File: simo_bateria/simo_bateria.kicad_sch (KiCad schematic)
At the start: 5 parts, among them J1 CONECTOR BATERIA( 8V), J2 CONECTOR PLUG IN (5V), U3 conversor_dc

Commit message: update placa simo bateria
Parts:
- BAT2: DIGIKEY (none) -> BK-18650-PC2-ND
- U3: NUMBER IC (none) -> 2156-LM2596SX-ADJ-TI-ND
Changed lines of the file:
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@@
       (effects (font (size 1.27 1.27)) hide)
     )
-    (property "Datasheet" "" (id 3) (at 84.582 53.34 0)
+    (property "Datasheet" "https://rocelec.widen.net/view/pdf/gzjkwe71dm/lm2596.pdf?t.download=true&u=5oefqw" (id 3) (at 84.582 53.34 0)
+      (effects (font (size 1.27 1.27)) hide)
+    )
+    (property "NUMBER IC" "2156-LM2596SX-ADJ-TI-ND" (id 4) (at 84.582 53.34 0)
       (effects (font (size 1.27 1.27)) hide)
     )
@@
       (effects (font (size 1.27 1.27)) hide)
     )
-    (property "Datasheet" "" (id 3) (at 45.466 62.357 0)
+    (property "Datasheet" "https://www.memoryprotectiondevices.com/datasheets/BK-18650-PC2-datasheet.pdf" (id 3) (at 45.466 62.357 0)
       (effects (font (size 1.27 1.27)) hide)
     )
+    (property "DIGIKEY" "BK-18650-PC2-ND" (id 4) (at 45.466 62.357 0)
+      (effects (font (size 1.27 1.27)) hide)
+    )

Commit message: Se hizo refactory del proyecto simo_bateria
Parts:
- removed BAT1, BAT2: bateria, Battery:BatteryHolder_MPD_BH-18650-PC2, symbol simo_bateria:bateria
- removed U3: conversor_dc, simo_bateria:conversor_dc_dc, symbol simo_bateria:conversor_dc
- added 11: conversor_dc_1_1, symbol simo_bateria:conversor_dc_1_1
- added BT1, BT2: Battery_Cell, simo_bateria:BatteryHolder_MPD_BH-18650-PC2, symbol Device:Battery_Cell
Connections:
- net at J1.2 (Pin_2): now also 11.1 (VIN-), BT2.2 (-)
- net at J2.1 (Pin_1): now also 11.2 (VOUT-)
- net at J2.2 (Pin_2): now also 11.4 (VOUT+)
- net at J1.1 (Pin_1): now also 11.3 (VIN+), BT1.1 (+)
- new net: BT1.2 (-), BT2.1 (+)
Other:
- note added: "Baterias en serie. 8,4 V MAX"
- note added: "PLUGIN ALIMENTA PLACA ELEMON"
- moved on the sheet: J1

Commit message: update simo_bateria
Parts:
- 11: footprint (none) -> simo_bateria:conversor_dc_dc
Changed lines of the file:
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@@
     (property "Reference" "11" (id 0) (at 95.377 50.8 0))
     (property "Value" "conversor_dc_1_1" (id 1) (at 95.377 53.34 0))
-    (property "Footprint" "" (id 2) (at 84.582 53.34 0)
+    (property "Footprint" "simo_bateria:conversor_dc_dc" (id 2) (at 84.582 53.34 0)
       (effects (font (size 1.27 1.27)) hide)
     )
@@
     )
     (path "/11fd5699-de88-4095-a2ac-268b5557a2ec"
-      (reference "11") (unit 1) (value "conversor_dc_1_1") (footprint "")
+      (reference "11") (unit 1) (value "conversor_dc_1_1") (footprint "simo_bateria:conversor_dc_dc")
     )
     (path "/0e1c8888-24a9-448a-8220-c54ef612d9ed"

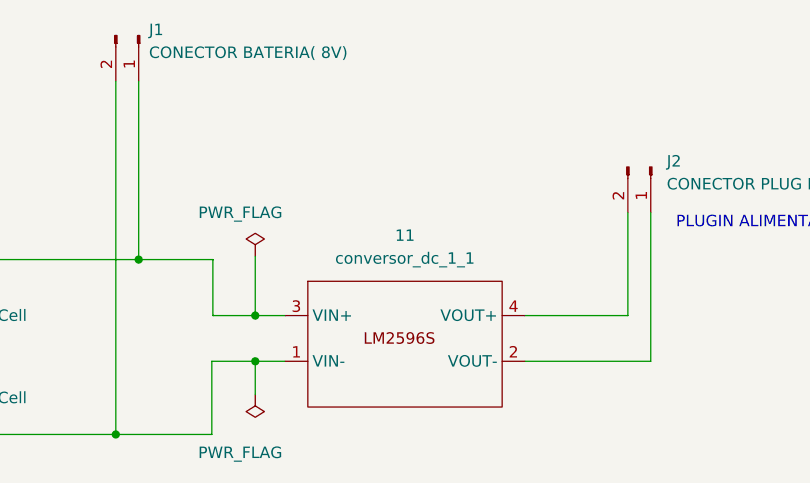
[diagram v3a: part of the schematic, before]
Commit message: update en ambas placas. Cambio de formato de carpetas. Footprint asignado pero modelos 3d aun no.
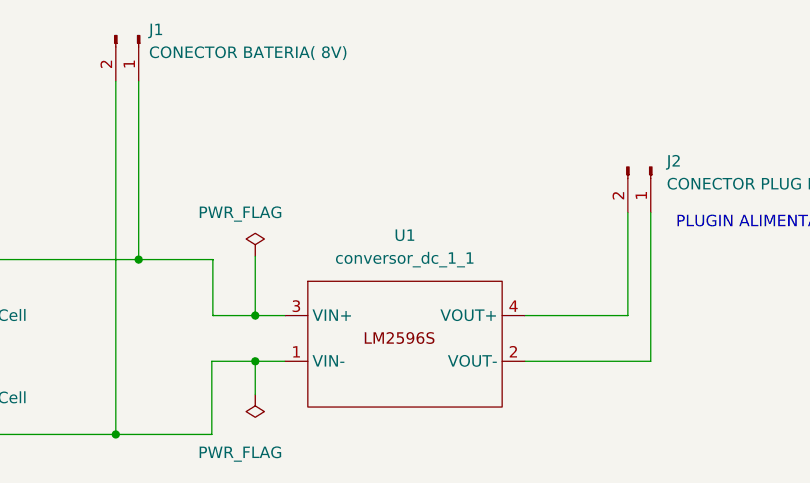
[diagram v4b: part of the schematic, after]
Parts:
- J1, J2: footprint Connector_JST:JST_EH_B2B-EH-A_1x02_P2.50mm_Vertical -> simo_bateria:JST_EH_B2B-EH-A_1x02_P2.50mm_Vertical
- renumbered 11 to U1
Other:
- title: Simo bateria -> Simo bateria, PCB de conexion
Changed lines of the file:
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@@
   (paper "A4")
   (title_block
-    (title "Simo bateria")
+    (title "Simo bateria, PCB de conexion")
     (date "2022-06-29")
-    (rev "Gusta Rodriguez")
+    (rev "0001")
     (company "I.N.T.I")
-    (comment 1 "Autor: German Velardez")
+    (comment 1 "Revisor: Gustavo Rodriguez")
+    (comment 2 "Autor:   German Velardez")
+    (comment 3 "Licencia: CERN Open Hardware Licence Version 2")
+    (comment 4 "Placa de conexion para elementos de la bateria.")
   )
   (junction (at 78.74 64.77) (diameter 0) (color 0 0 0 0)
@@
   (symbol (lib_id "simo_bateria:conversor_dc_1_1") (at 84.582 53.34 0) (unit 1)
     (in_bom yes) (on_board yes) (fields_autoplaced)
-    (property "Reference" "11" (id 0) (at 95.377 50.8 0))
+    (property "Reference" "U1" (id 0) (at 95.377 50.8 0))
     (property "Value" "conversor_dc_1_1" (id 1) (at 95.377 53.34 0))
     (property "Footprint" "simo_bateria:conversor_dc_dc" (id 2) (at 84.582 53.34 0)
@@
       (effects (font (size 1.27 1.27)) (justify left))
     )
-    (property "Footprint" "Connector_JST:JST_EH_B2B-EH-A_1x02_P2.50mm_Vertical" (id 2) (at 122.682 43.18 0)
+    (property "Footprint" "simo_bateria:JST_EH_B2B-EH-A_1x02_P2.50mm_Vertical" (id 2) (at 122.682 43.18 0)
       (effects (font (size 1.27 1.27)) hide)
     )
@@
       (effects (font (size 1.27 1.27)) (justify left))
     )
-    (property "Footprint" "Connector_JST:JST_EH_B2B-EH-A_1x02_P2.50mm_Vertical" (id 2) (at 65.786 28.575 0)
+    (property "Footprint" "simo_bateria:JST_EH_B2B-EH-A_1x02_P2.50mm_Vertical" (id 2) (at 65.786 28.575 0)
       (effects (font (size 1.27 1.27)) hide)
     )
@@
       (reference "#FLG0102") (unit 1) (value "PWR_FLAG") (footprint "")
     )
-    (path "/11fd5699-de88-4095-a2ac-268b5557a2ec"
-      (reference "11") (unit 1) (value "conversor_dc_1_1") (footprint "simo_bateria:conversor_dc_dc")
-    )
     (path "/0e1c8888-24a9-448a-8220-c54ef612d9ed"
       (reference "BT1") (unit 1) (value "Battery_Cell") (footprint "simo_bateria:BatteryHolder_MPD_BH-18650-PC2")
@@
     )
     (path "/cd0b3651-2ed3-41e3-88cd-89e3b9462bf8"
-      (reference "J1") (unit 1) (value "CONECTOR BATERIA( 8V)") (footprint "Connector_JST:JST_EH_B2B-EH-A_1x02_P2.50mm_Vertical")
+      (reference "J1") (unit 1) (value "CONECTOR BATERIA( 8V)") (footprint "simo_bateria:JST_EH_B2B-EH-A_1x02_P2.50mm_Vertical")
     )
     (path "/94003890-1ebb-4a1a-91b8-849e4df6bd6b"
-      (reference "J2") (unit 1) (value "CONECTOR PLUG IN (5V)") (footprint "Connector_JST:JST_EH_B2B-EH-A_1x02_P2.50mm_Vertical")
-    )
-  )
+      (reference "J2") (unit 1) (value "CONECTOR PLUG IN (5V)") (footprint "simo_bateria:JST_EH_B2B-EH-A_1x02_P2.50mm_Vertical")
+    )
+    (path "/11fd5699-de88-4095-a2ac-268b5557a2ec"
+      (reference "U1") (unit 1) (value "conversor_dc_1_1") (footprint "simo_bateria:conversor_dc_dc")
+    )
+  )

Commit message: update en ambas placas, revision 02
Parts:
- removed J1: CONECTOR BATERIA( 8V), simo_bateria:JST_EH_B2B-EH-A_1x02_P2.50mm_Vertical, symbol Connector:Conn_01x02_Male
- removed J2: CONECTOR PLUG IN (5V), simo_bateria:JST_EH_B2B-EH-A_1x02_P2.50mm_Vertical, symbol Connector:Conn_01x02_Male
- added J1, J2: conector_bateria, simo_bateria:JST_EH_B2B-EH-A_1x02_P2.50mm_Vertical, symbol simo_bateria:conector_bateria
- added R1: 355k, Resistor_SMD:R_0805_2012Metric_Pad1.20x1.40mm_HandSolder, symbol Device:R
- added R2: 155k, Resistor_SMD:R_0805_2012Metric_Pad1.20x1.40mm_HandSolder, symbol Device:R
- BT1: footprint simo_bateria:BatteryHolder_MPD_BH-18650-PC2 -> resistores:trimmer_bourns_3250w
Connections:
- net at BT1.1 (+), U1.3 (VIN+): now also J1.1 (Pin_1), R1.1
- net at BT2.2 (-), U1.1 (VIN-): now also J1.2 (Pin_2), R2.2
- net at U1.2 (VOUT-): now also J2.2 (Pin_2)
- net at U1.4 (VOUT+): now also J2.1 (Pin_1)
- new net: R1.2, R2.1
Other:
- note added: "1 LEVEL (VBAT SIN REGULADOR) 2 GND"
- note added: "CONECTOR LEVEL DE BATERIA DEBE AJUSTARSE A TENSION MENOR A 3.3V."
- note added: "MEDICION DE NIVEL DE BATERIA (PIN LEVEL)"
- note added: "REGULADOR DE ALIMENTACION"
- moved on the sheet: BT1, BT2, U1

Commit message: update 2. Listo para revision 2
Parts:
- BT1: footprint resistores:trimmer_bourns_3250w -> simo_bateria:BatteryHolder_MPD_BH-18650-PC2
- R1, R2: footprint Resistor_SMD:R_0805_2012Metric_Pad1.20x1.40mm_HandSolder -> simo_bateria:R_0805_2012Metric_Pad1.20x1.40mm_HandSolder
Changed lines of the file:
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@@
       (effects (font (size 1.27 1.27)) (justify left))
     )
-    (property "Footprint" "resistores:trimmer_bourns_3250w" (id 2) (at 133.35 97.536 90)
+    (property "Footprint" "simo_bateria:BatteryHolder_MPD_BH-18650-PC2" (id 2) (at 133.35 97.536 90)
       (effects (font (size 1.27 1.27)) hide)
     )
@@
       (effects (font (size 1.27 1.27)) (justify left))
     )
-    (property "Footprint" "Resistor_SMD:R_0805_2012Metric_Pad1.20x1.40mm_HandSolder" (id 2) (at 99.822 105.41 90)
+    (property "Footprint" "simo_bateria:R_0805_2012Metric_Pad1.20x1.40mm_HandSolder" (id 2) (at 99.822 105.41 90)
       (effects (font (size 1.27 1.27)) hide)
     )
@@
       (effects (font (size 1.27 1.27)) (justify left))
     )
-    (property "Footprint" "Resistor_SMD:R_0805_2012Metric_Pad1.20x1.40mm_HandSolder" (id 2) (at 99.822 96.52 90)
+    (property "Footprint" "simo_bateria:R_0805_2012Metric_Pad1.20x1.40mm_HandSolder" (id 2) (at 99.822 96.52 90)
       (effects (font (size 1.27 1.27)) hide)
     )
@@
     )
     (path "/0e1c8888-24a9-448a-8220-c54ef612d9ed"
-      (reference "BT1") (unit 1) (value "Battery_Cell") (footprint "resistores:trimmer_bourns_3250w")
+      (reference "BT1") (unit 1) (value "Battery_Cell") (footprint "simo_bateria:BatteryHolder_MPD_BH-18650-PC2")
     )
     (path "/6ee16ed8-9642-4dca-a183-41d6990007c4"
@@
     )
     (path "/8da78f3b-5575-47f1-9326-e93636a9e26c"
-      (reference "R1") (unit 1) (value "355k") (footprint "Resistor_SMD:R_0805_2012Metric_Pad1.20x1.40mm_HandSolder")
+      (reference "R1") (unit 1) (value "355k") (footprint "simo_bateria:R_0805_2012Metric_Pad1.20x1.40mm_HandSolder")
     )
     (path "/2a9711d0-b0e4-422e-9cee-c254b4155632"
-      (reference "R2") (unit 1) (value "155k") (footprint "Resistor_SMD:R_0805_2012Metric_Pad1.20x1.40mm_HandSolder")
+      (reference "R2") (unit 1) (value "155k") (footprint "simo_bateria:R_0805_2012Metric_Pad1.20x1.40mm_HandSolder")
     )
     (path "/11fd5699-de88-4095-a2ac-268b5557a2ec"

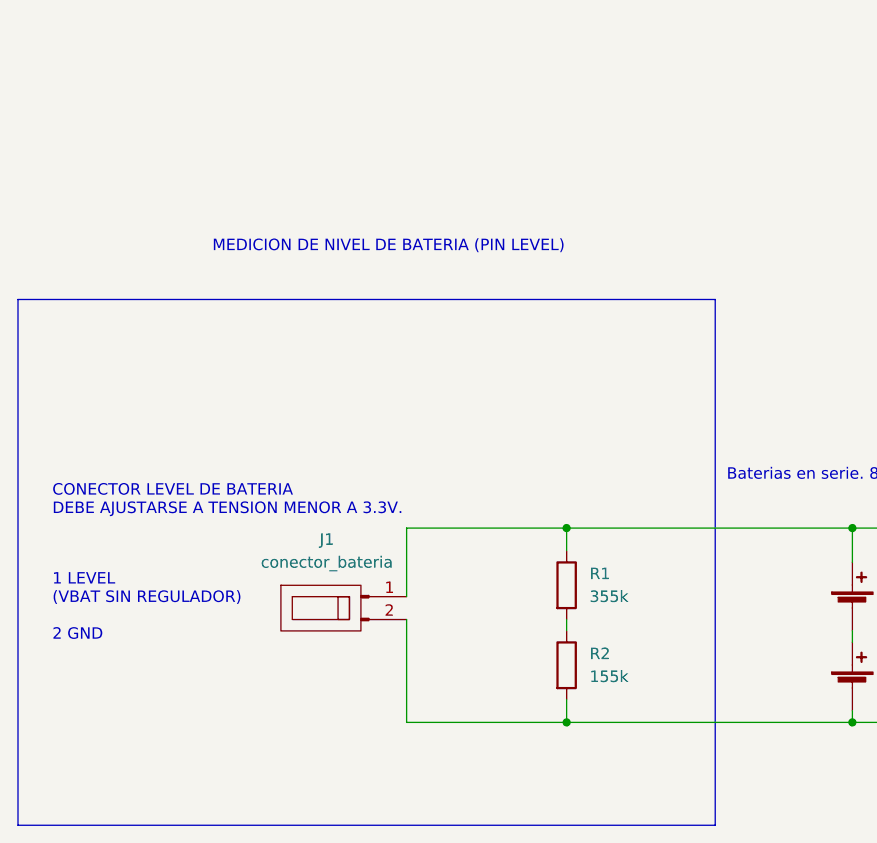
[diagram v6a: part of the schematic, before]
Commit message: modificaciones menores en placa simo bateria. La salida del divisor de tension estaba mal ubicada.
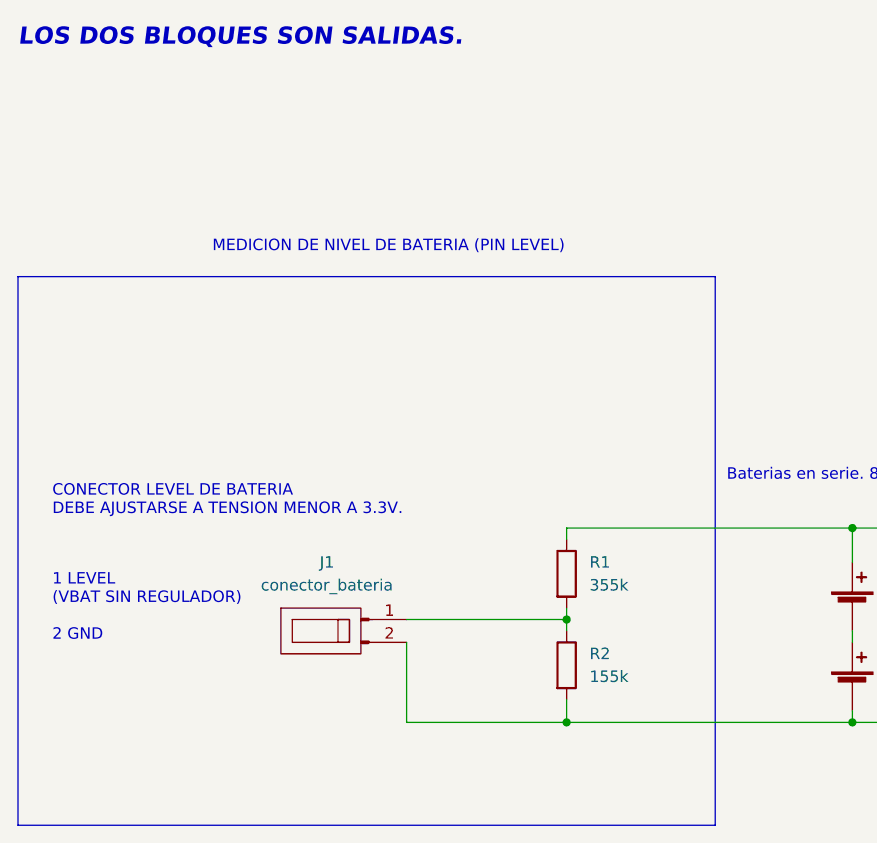
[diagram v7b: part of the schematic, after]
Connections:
- net at BT1.1 (+), R1.1, U1.3 (VIN+): no longer J1.1 (Pin_1)
- net at R1.2, R2.1: now also J1.1 (Pin_1)
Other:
- note added: "LOS DOS BLOQUES SON SALIDAS."
- moved on the sheet: J1, R1
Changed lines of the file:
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@@
     (comment 4 "Placa de conexion para elementos de la bateria.")
   )
-  (junction (at 101.6 90.17) (diameter 0) (color 0 0 0 0)
+  (junction (at 101.6 100.33) (diameter 0) (color 0 0 0 0)
   )
   (junction (at 101.6 111.76) (diameter 0) (color 0 0 0 0)
@@
   (junction (at 167.64 90.17) (diameter 0) (color 0 0 0 0)
   )
-  (polyline (pts (xy 40.64 64.77) (xy 118.11 64.77))
+  (polyline (pts (xy 40.64 62.23) (xy 118.11 62.23))
     (stroke (width 0) (type default) (color 0 0 0 0))
   )
@@
     (stroke (width 0) (type default) (color 0 0 0 0))
   )
-  (wire (pts (xy 101.6 90.17) (xy 101.6 92.71))
+  (wire (pts (xy 101.6 90.17) (xy 101.6 91.44))
     (stroke (width 0) (type default) (color 0 0 0 0))
   )
@@
     (stroke (width 0) (type default) (color 0 0 0 0))
   )
+  (wire (pts (xy 101.6 100.33) (xy 101.6 101.6))
+    (stroke (width 0) (type default) (color 0 0 0 0))
+  )
   (wire (pts (xy 101.6 109.22) (xy 101.6 111.76))
     (stroke (width 0) (type default) (color 0 0 0 0))
   )
+  (wire (pts (xy 83.82 100.33) (xy 101.6 100.33))
+    (stroke (width 0) (type default) (color 0 0 0 0))
+  )
   (wire (pts (xy 133.35 111.76) (xy 167.64 111.76))
     (stroke (width 0) (type default) (color 0 0 0 0))
@@
     (stroke (width 0) (type default) (color 0 0 0 0))
   )
-  (wire (pts (xy 101.6 100.33) (xy 101.6 101.6))
+  (wire (pts (xy 101.6 99.06) (xy 101.6 100.33))
     (stroke (width 0) (type default) (color 0 0 0 0))
   )
@@
     (stroke (width 0) (type default) (color 0 0 0 0))
   )
-  (polyline (pts (xy 118.11 64.77) (xy 118.11 123.19))
+  (polyline (pts (xy 118.11 62.23) (xy 118.11 123.19))
     (stroke (width 0) (type default) (color 0 0 0 0))
   )
@@
     (stroke (width 0) (type default) (color 0 0 0 0))
   )
-  (polyline (pts (xy 40.64 123.19) (xy 40.64 64.77))
+  (polyline (pts (xy 40.64 123.19) (xy 40.64 62.23))
     (stroke (width 0) (type default) (color 0 0 0 0))
   )
@@
     (stroke (width 0) (type default) (color 0 0 0 0))
   )
-  (wire (pts (xy 83.82 90.17) (xy 83.82 97.79))
-    (stroke (width 0) (type default) (color 0 0 0 0))
-  )
   (wire (pts (xy 83.82 111.76) (xy 101.6 111.76))
     (stroke (width 0) (type default) (color 0 0 0 0))
   )
-  (wire (pts (xy 101.6 90.17) (xy 83.82 90.17))
-    (stroke (width 0) (type default) (color 0 0 0 0))
-  )
-  (wire (pts (xy 83.82 100.33) (xy 83.82 111.76))
+  (wire (pts (xy 83.82 102.87) (xy 83.82 111.76))
     (stroke (width 0) (type default) (color 0 0 0 0))
   )
@@
     (effects (font (size 1.27 1.27)) (justify left bottom))
   )
+  (text "LOS DOS BLOQUES SON SALIDAS." (at 40.64 36.83 0)
+    (effects (font (size 1.905 1.905) (thickness 0.381) bold italic) (justify left bottom))
+  )
   (text "1 LEVEL \n(VBAT SIN REGULADOR)\n\n2 GND\n" (at 44.45 102.87 0)
     (effects (font (size 1.27 1.27)) (justify left bottom))
@@
       (effects (font (size 1.27 1.27)) hide)
     )
-    (property "Datasheet" "~" (id 3) (at 133.35 97.536 90)
+    (property "Datasheet" "https://www.memoryprotectiondevices.com/datasheets/BK-18650-PC2-datasheet.pdf" (id 3) (at 133.35 97.536 90)
       (effects (font (size 1.27 1.27)) hide)
     )
@@
       (effects (font (size 1.27 1.27)) hide)
     )
-    (property "Datasheet" "" (id 3) (at 173.99 90.17 0)
+    (property "Datasheet" "https://pdf1.alldatasheet.com/datasheet-pdf/view/529273/TI1/LM2596S-12.html" (id 3) (at 173.99 90.17 0)
       (effects (font (size 1.27 1.27)) hide)
     )
@@
       (effects (font (size 1.27 1.27)) hide)
     )
-    (property "Datasheet" "~" (id 3) (at 209.55 76.2 0)
+    (property "Datasheet" "https://docs.rs-online.com/7ac3/0900766b8159469c.pdf" (id 3) (at 209.55 76.2 0)
       (effects (font (size 1.27 1.27)) hide)
     )
@@
       (effects (font (size 1.27 1.27)) hide)
     )
-    (property "Datasheet" "~" (id 3) (at 133.35 106.426 90)
-      (effects (font (size 1.27 1.27)) hide)
-    )
-    (pin "1")
-    (pin "2")
-  )
-  (symbol (lib_id "Device:R") (at 101.6 96.52 0) (unit 1)
-    (in_bom yes) (on_board yes) (fields_autoplaced)
-    (property "Reference" "R1" (id 0) (at 104.14 95.2499 0)
-      (effects (font (size 1.27 1.27)) (justify left))
-    )
-    (property "Value" "355k" (id 1) (at 104.14 97.7899 0)
-      (effects (font (size 1.27 1.27)) (justify left))
-    )
-    (property "Footprint" "simo_bateria:R_0805_2012Metric_Pad1.20x1.40mm_HandSolder" (id 2) (at 99.822 96.52 90)
-      (effects (font (size 1.27 1.27)) hide)
-    )
-    (property "Datasheet" "~" (id 3) (at 101.6 96.52 0)
+    (property "Datasheet" "https://www.memoryprotectiondevices.com/datasheets/BK-18650-PC2-datasheet.pdf" (id 3) (at 133.35 106.426 90)
+      (effects (font (size 1.27 1.27)) hide)
+    )
+    (pin "1")
+    (pin "2")
+  )
+  (symbol (lib_id "Device:R") (at 101.6 95.25 0) (unit 1)
+    (in_bom yes) (on_board yes) (fields_autoplaced)
+    (property "Reference" "R1" (id 0) (at 104.14 93.9799 0)
+      (effects (font (size 1.27 1.27)) (justify left))
+    )
+    (property "Value" "355k" (id 1) (at 104.14 96.5199 0)
+      (effects (font (size 1.27 1.27)) (justify left))
+    )
+    (property "Footprint" "simo_bateria:R_0805_2012Metric_Pad1.20x1.40mm_HandSolder" (id 2) (at 99.822 95.25 90)
+      (effects (font (size 1.27 1.27)) hide)
+    )
+    (property "Datasheet" "~" (id 3) (at 101.6 95.25 0)
       (effects (font (size 1.27 1.27)) hide)
     )
@@
     (pin "1")
   )
-  (symbol (lib_id "simo_bateria:conector_bateria") (at 78.74 97.79 0) (unit 1)
-    (in_bom yes) (on_board yes) (fields_autoplaced)
-    (property "Reference" "J1" (id 0) (at 74.9681 91.44 0))
-    (property "Value" "conector_bateria" (id 1) (at 74.9681 93.98 0))
-    (property "Footprint" "simo_bateria:JST_EH_B2B-EH-A_1x02_P2.50mm_Vertical" (id 2) (at 78.74 90.17 0)
-      (effects (font (size 1.27 1.27)) hide)
-    )
-    (property "Datasheet" "~" (id 3) (at 78.74 97.79 0)
-      (effects (font (size 1.27 1.27)) hide)
-    )
+  (symbol (lib_id "simo_bateria:conector_bateria") (at 78.74 100.33 0) (unit 1)
+    (in_bom yes) (on_board yes) (fields_autoplaced)
+    (property "Reference" "J1" (id 0) (at 74.9681 93.98 0))
+    (property "Value" "conector_bateria" (id 1) (at 74.9681 96.52 0))
+    (property "Footprint" "simo_bateria:JST_EH_B2B-EH-A_1x02_P2.50mm_Vertical" (id 2) (at 78.74 92.71 0)
+      (effects (font (size 1.27 1.27)) hide)
+    )
+    (property "Datasheet" "https://docs.rs-online.com/7ac3/0900766b8159469c.pdf" (id 3) (at 78.74 100.33 0)
+      (effects (font (size 1.27 1.27)) hide)
+    )
